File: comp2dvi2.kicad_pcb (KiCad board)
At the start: 2 copper layers, 44.1 x 62 mm, 37 parts, among them J1 Conn_Coaxial, J2 Conn_Coaxial, J3 Conn_Coaxial, J4 USB_B_Micro, J5 DVI-I-R, SW1 SW_DIP_x02, SW2 SW_DPDT_x2, U1 THS7368

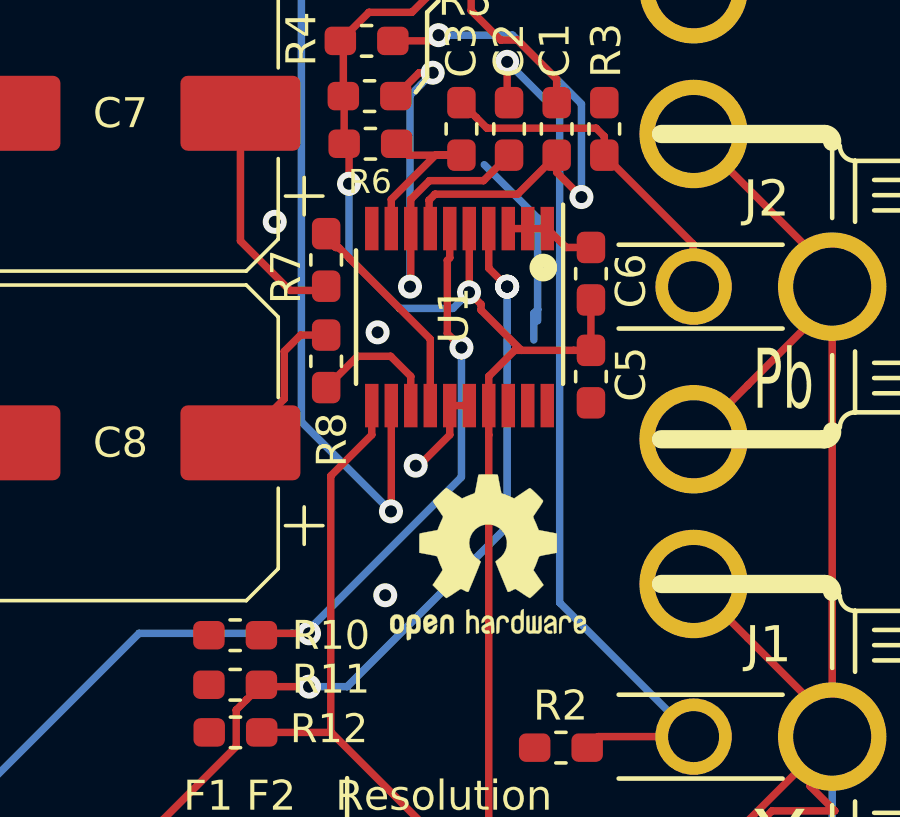
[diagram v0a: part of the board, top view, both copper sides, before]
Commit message: Bypass Cap Routing
Fixed routing so that the power from the USB goes to the 100nF bypass cap before hitting the chip. Thanks to Tianfeng for pointing this out. Gerbers updated as well.
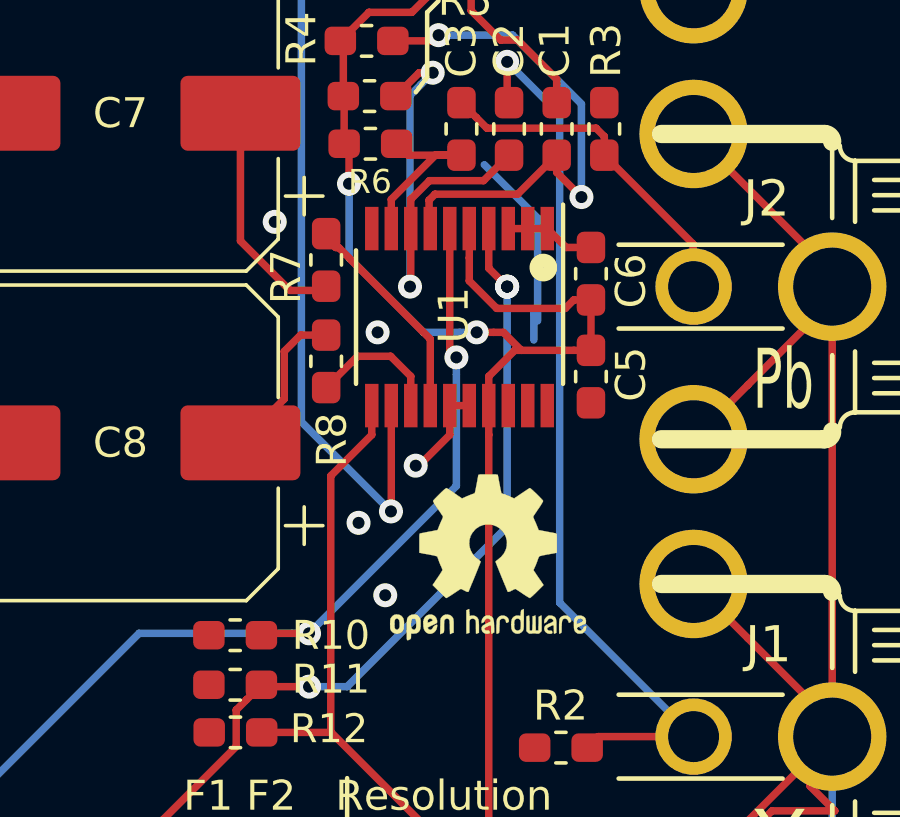
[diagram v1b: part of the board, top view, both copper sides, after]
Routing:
- net 5V: track 85.4 -> 89.1 mm
- net GND: vias 6 -> 7
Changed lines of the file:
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@@
     (thickness 1.6)
     (drawings 23)
-    (tracks 273)
+    (tracks 276)
     (zones 0)
     (modules 37)
@@
   (segment (start 95.9075 95.914) (end 95.9075 94.939) (width 0.25) (layer F.Cu) (net 7))
   (segment (start 99.314 94.0715) (end 99.314 92.3925) (width 0.25) (layer F.Cu) (net 7))
-  (via (at 95.25 92.1385) (size 0.8) (drill 0.4) (layers F.Cu B.Cu) (net 7))
-  (segment (start 95.2575 90.014) (end 95.2575 92.131) (width 0.25) (layer F.Cu) (net 7))
-  (segment (start 95.2575 92.131) (end 95.25 92.1385) (width 0.25) (layer F.Cu) (net 7))
   (via (at 91.2495 88.519) (size 0.8) (drill 0.4) (layers F.Cu B.Cu) (net 7))
-  (segment (start 91.2495 90.989002) (end 91.2495 88.519) (width 0.25) (layer B.Cu) (net 7))
-  (segment (start 92.933499 92.673001) (end 91.2495 90.989002) (width 0.25) (layer B.Cu) (net 7))
-  (segment (start 95.25 92.1385) (end 94.715499 92.673001) (width 0.25) (layer B.Cu) (net 7))
-  (segment (start 94.715499 92.673001) (end 92.933499 92.673001) (width 0.25) (layer B.Cu) (net 7))
   (segment (start 91.2495 87.348) (end 91.087 87.1855) (width 0.25) (layer F.Cu) (net 7))
   (segment (start 91.2495 88.519) (end 91.2495 87.348) (width 0.25) (layer F.Cu) (net 7))
-  (segment (start 95.649999 92.728999) (end 96.9925 94.0715) (width 0.25) (layer F.Cu) (net 7))
-  (segment (start 95.649999 92.538499) (end 95.649999 92.728999) (width 0.25) (layer F.Cu) (net 7))
-  (segment (start 95.25 92.1385) (end 95.649999 92.538499) (width 0.25) (layer F.Cu) (net 7))
   (segment (start 96.775 94.0715) (end 96.9925 94.0715) (width 0.25) (layer F.Cu) (net 7))
   (segment (start 96.9925 94.0715) (end 98.739 94.0715) (width 0.25) (layer F.Cu) (net 7))
@@
   (segment (start 93.069 70.027) (end 94.516 68.58) (width 0.25) (layer F.Cu) (net 7))
   (segment (start 93.069 73.914) (end 93.069 70.027) (width 0.25) (layer F.Cu) (net 7))
+  (segment (start 93.732498 93.472) (end 94.938315 93.472) (width 0.25) (layer B.Cu) (net 7))
+  (segment (start 91.2495 88.519) (end 91.2495 90.989002) (width 0.25) (layer B.Cu) (net 7))
+  (segment (start 94.938315 93.472) (end 95.504 93.472) (width 0.25) (layer B.Cu) (net 7))
+  (segment (start 96.069685 93.472) (end 95.504 93.472) (width 0.25) (layer F.Cu) (net 7))
+  (segment (start 91.2495 90.989002) (end 93.732498 93.472) (width 0.25) (layer B.Cu) (net 7))
+  (segment (start 96.393 93.472) (end 96.069685 93.472) (width 0.25) (layer F.Cu) (net 7))
+  (segment (start 96.9925 94.0715) (end 96.393 93.472) (width 0.25) (layer F.Cu) (net 7))
+  (via (at 95.504 93.472) (size 0.8) (drill 0.4) (layers F.Cu B.Cu) (net 7))
+  (segment (start 95.2575 90.989) (end 95.2575 90.014) (width 0.25) (layer F.Cu) (net 7))
+  (segment (start 95.2575 91.758502) (end 95.2575 90.989) (width 0.25) (layer F.Cu) (net 7))
+  (segment (start 96.171999 92.673001) (end 95.2575 91.758502) (width 0.25) (layer F.Cu) (net 7))
+  (segment (start 98.458499 92.673001) (end 96.171999 92.673001) (width 0.25) (layer F.Cu) (net 7))
+  (segment (start 98.739 92.3925) (end 98.458499 92.673001) (width 0.25) (layer F.Cu) (net 7))
+  (segment (start 99.314 92.3925) (end 98.739 92.3925) (width 0.25) (layer F.Cu) (net 7))
   (via (at 92.202 93.472) (size 0.8) (drill 0.4) (layers F.Cu B.Cu) (net 8))
   (via (at 88.773 89.789) (size 0.8) (drill 0.4) (layers F.Cu B.Cu) (net 8))
@@
   (segment (start 71.12 117.487) (end 71.12 109.743498) (width 0.25) (layer B.Cu) (net 8))
   (segment (start 70.159 118.448) (end 71.12 117.487) (width 0.25) (layer B.Cu) (net 8))
+  (via (at 91.567 99.822) (size 0.8) (drill 0.4) (layers F.Cu B.Cu) (net 8))
   (segment (start 75.310999 98.298001) (end 74.676 98.933) (width 0.25) (layer F.Cu) (net 9))
   (segment (start 77.30449 96.30451) (end 75.310999 98.298001) (width 0.25) (layer F.Cu) (net 9))
@@
   (segment (start 93.3075 95.914) (end 93.3075 94.939) (width 0.25) (layer F.Cu) (net 37))
   (segment (start 93.3075 94.939) (end 92.638 94.2695) (width 0.25) (layer F.Cu) (net 37))
-  (via (at 94.996 93.98) (size 0.8) (drill 0.4) (layers F.Cu B.Cu) (net 38))
-  (segment (start 94.524999 93.508999) (end 94.996 93.98) (width 0.25) (layer F.Cu) (net 38))
-  (segment (start 94.524999 91.071501) (end 94.524999 93.508999) (width 0.25) (layer F.Cu) (net 38))
-  (segment (start 94.6075 90.014) (end 94.6075 90.989) (width 0.25) (layer F.Cu) (net 38))
-  (segment (start 94.6075 90.989) (end 94.524999 91.071501) (width 0.25) (layer F.Cu) (net 38))
   (via (at 89.916 103.505) (size 0.8) (drill 0.4) (layers F.Cu B.Cu) (net 38))
-  (segment (start 89.916 103.378) (end 89.916 103.505) (width 0.25) (layer B.Cu) (net 38))
-  (segment (start 94.996 93.98) (end 94.996 98.298) (width 0.25) (layer B.Cu) (net 38))
-  (segment (start 94.996 98.298) (end 89.916 103.378) (width 0.25) (layer B.Cu) (net 38))
   (segment (start 88.392 103.505) (end 88.3285 103.5685) (width 0.25) (layer F.Cu) (net 38))
   (segment (start 89.916 103.505) (end 88.392 103.505) (width 0.25) (layer F.Cu) (net 38))
@@
   (segment (start 80.645 121.0564) (end 80.645 120.0064) (width 0.25) (layer B.Cu) (net 38))
   (segment (start 80.645 120.0064) (end 78.7908 118.1522) (width 0.25) (layer B.Cu) (net 38))
+  (segment (start 89.916 103.505) (end 94.82807 98.59293) (width 0.25) (layer B.Cu) (net 38))
+  (segment (start 94.6075 90.014) (end 94.6075 94.087312) (width 0.25) (layer F.Cu) (net 38))
+  (segment (start 94.82807 94.873567) (end 94.82807 94.307882) (width 0.25) (layer B.Cu) (net 38))
+  (segment (start 94.6075 94.087312) (end 94.82807 94.307882) (width 0.25) (layer F.Cu) (net 38))
+  (segment (start 94.82807 98.59293) (end 94.82807 94.873567) (width 0.25) (layer B.Cu) (net 38))
+  (via (at 94.82807 94.307882) (size 0.8) (drill 0.4) (layers F.Cu B.Cu) (net 38))
   (via (at 96.52 91.948) (size 0.8) (drill 0.4) (layers F.Cu B.Cu) (net 39))
   (segment (start 95.9075 90.014) (end 95.9075 91.3355) (width 0.25) (layer F.Cu) (net 39))
